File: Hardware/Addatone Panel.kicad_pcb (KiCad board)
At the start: 2 copper layers, 60.8 x 128.5 mm, 36 parts, among them J3 PItch_In, J4 Harm1_In, J5 Harm2_In, J6 Freq_Scale_In, J7 DAC1_Out, J8 DAC2_Out, SW1 SW_Push, SW2 SW_Push, SW3 SW_SPST, SW4 SW_SPST

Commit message: Further updates to PCBs
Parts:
- added G***: LOGO, Graphics:Addatone, B.Cu at (130.0, 45.0)
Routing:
- removed copper zone on B.Cu, net GND
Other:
- board text added: "Fine"
- board text added: "Mountjoy Modular"
- board text added: "Tune"
- board text removed: "+1"
- board text removed: "+2"
- board text removed: "-1"
- board text removed: "-2"
- board text removed: "0"
- board text removed: "Fine Tune"

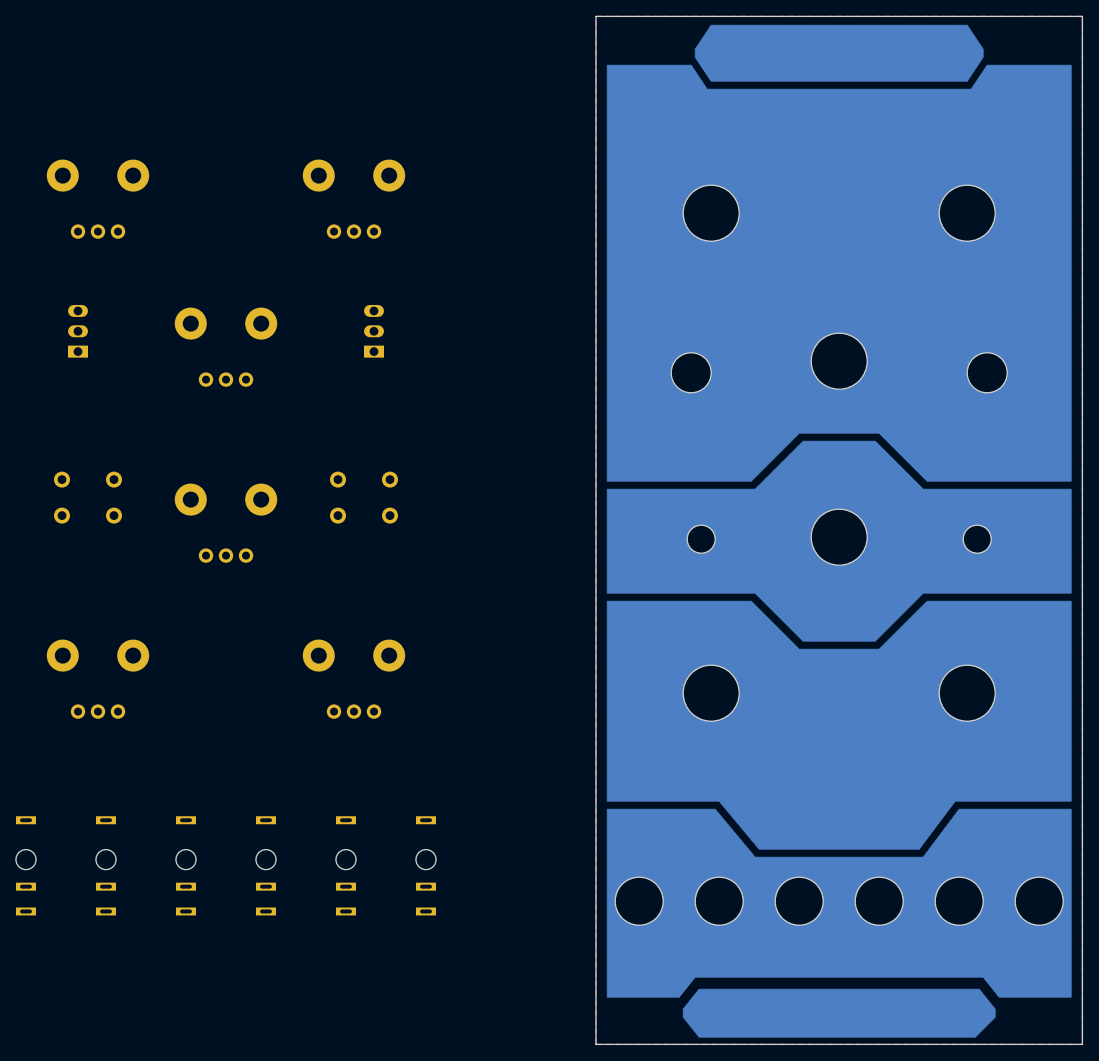
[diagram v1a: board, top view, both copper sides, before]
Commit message: Checking FPGA programming code and updated bitstream
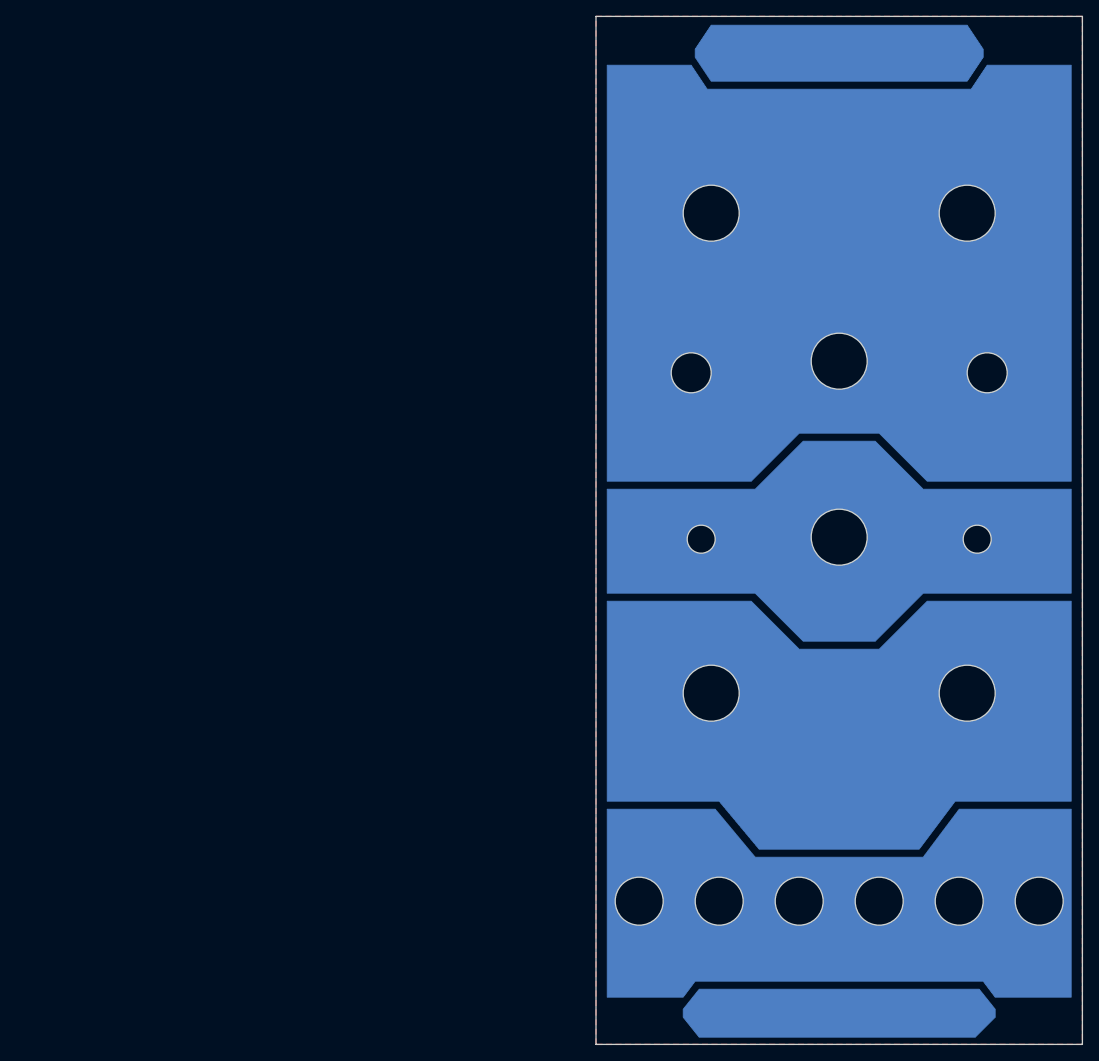
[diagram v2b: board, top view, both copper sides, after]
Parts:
- removed CTune1, FTune1, FreqScale1, Harm1, Harm2, HarmCount1: B10k, Custom_Footprints:Alpha_9mm_Potentiometer
- removed J3: PItch_In, Custom_Footprints:THONKICONN_hole
- removed J4: Harm1_In, Custom_Footprints:THONKICONN_hole
- removed J5: Harm2_In, Custom_Footprints:THONKICONN_hole
- removed J6: Freq_Scale_In, Custom_Footprints:THONKICONN_hole
- removed J7: DAC1_Out, Custom_Footprints:THONKICONN_hole
- removed J8: DAC2_Out, Custom_Footprints:THONKICONN_hole
- removed SW1, SW2: SW_Push, Buttons_Switches_THT:SW_PUSH_6mm
- removed SW3, SW4: SW_SPST, Custom_Footprints:SPDTSubMiniature

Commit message: Updates to PCB layout
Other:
- board text added: "Addatone Panel v1.0"
- board text added: "JLCJLCJLCJLC"
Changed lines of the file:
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@@
   (general
     (thickness 1.6)
-    (drawings 120)
+    (drawings 122)
     (tracks 0)
     (zones 0)
@@
   (page A4)
   (layers
-    (0 F.Cu signal)
-    (31 B.Cu signal)
+    (0 F.Cu signal hide)
+    (31 B.Cu signal hide)
     (32 B.Adhes user)
     (33 F.Adhes user hide)
@@
       (drillshape 0)
       (scaleselection 1)
-      (outputdirectory "Gerbers/PCB/"))
+      (outputdirectory "Gerbers/Panel/"))
   )
   (net 0 "")
@@
     (pad "" np_thru_hole oval (at 0 0) (size 5 3.2) (drill oval 5 3.2) (layers *.Cu *.Mask))
   )
+  (gr_text JLCJLCJLCJLC (at 130.5 161.4) (layer F.SilkS)
+    (effects (font (size 1 1) (thickness 0.15)))
+  )
+  (gr_text "Addatone Panel v1.0" (at 130.2 51.7) (layer F.SilkS)
+    (effects (font (size 2 2) (thickness 0.3)))
+  )
   (gr_line (start 113.4 49.6) (end 146.6 49.6) (layer B.Mask) (width 0.4))

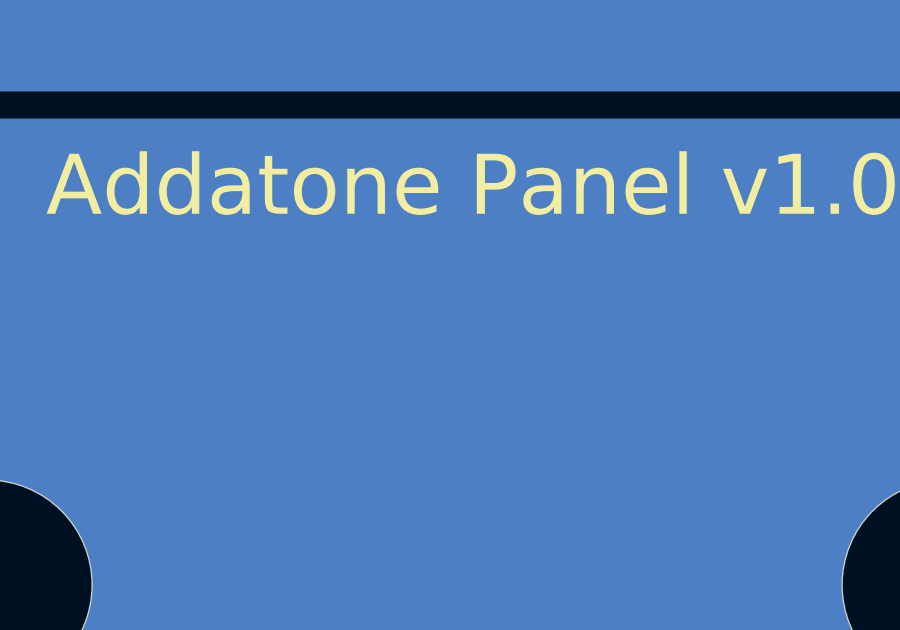
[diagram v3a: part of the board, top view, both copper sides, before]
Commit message: Fixes to schematic (missing resistor on 1.2V LDO); Created new implementation to support production board; added FPGA tester project
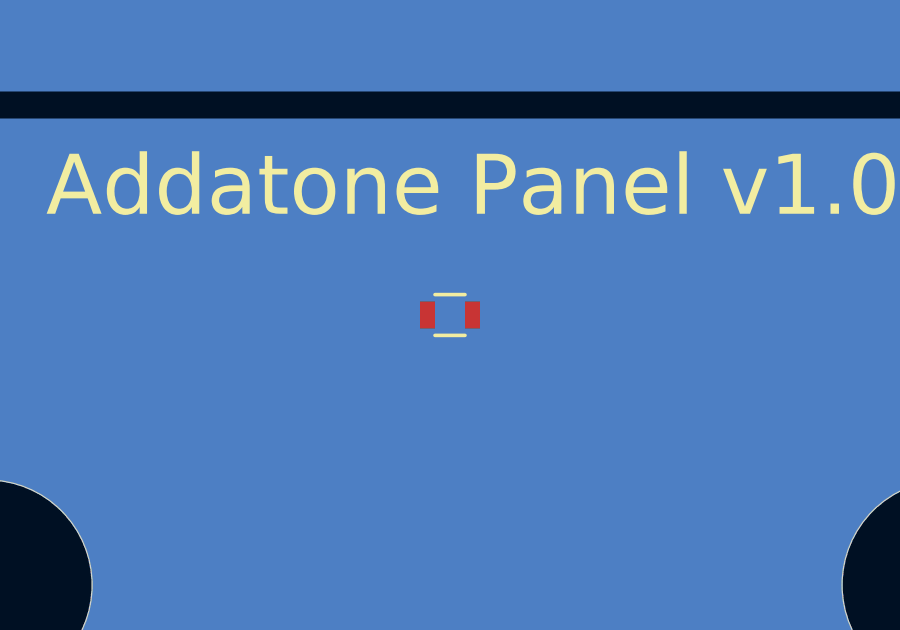
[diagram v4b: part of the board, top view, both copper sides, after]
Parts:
- added REF**: R_0603, Resistors_SMD:R_0603, F.Cu at (129.4, 56.0)
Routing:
- added copper zone on F.Cu, net (none)
- removed copper zone on F.Cu, net GND
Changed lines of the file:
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@@
     (tracks 0)
     (zones 0)
-    (modules 21)
-    (nets 2)
+    (modules 22)
+    (nets 1)
   )
   (page A4)
@@
   )
   (net 0 "")
-  (net 1 GND)
   (net_class Default "This is the default net class."
     (clearance 0.2)
@@
     (uvia_dia 0.3)
     (uvia_drill 0.1)
+  )
+  (module Resistors_SMD:R_0603 (layer F.Cu)
+    (at 129.43 56)
+    (descr "Resistor SMD 0603, reflow soldering, Vishay (see dcrcw.pdf)")
+    (tags "resistor 0603")
+    (attr smd)
+    (fp_text reference REF** (at 0 -1.45) (layer F.SilkS) hide
+      (effects (font (size 1 1) (thickness 0.15)))
+    )
+    (fp_text value R_0603 (at 0 1.5) (layer F.Fab)
+      (effects (font (size 1 1) (thickness 0.15)))
+    )
+    (fp_text user %R (at 0 0) (layer F.Fab)
+      (effects (font (size 0.4 0.4) (thickness 0.075)))
+    )
+    (fp_line (start -0.8 0.4) (end -0.8 -0.4) (layer F.Fab) (width 0.1))
+    (fp_line (start 0.8 0.4) (end -0.8 0.4) (layer F.Fab) (width 0.1))
+    (fp_line (start 0.8 -0.4) (end 0.8 0.4) (layer F.Fab) (width 0.1))
+    (fp_line (start -0.8 -0.4) (end 0.8 -0.4) (layer F.Fab) (width 0.1))
+    (fp_line (start 0.5 0.68) (end -0.5 0.68) (layer F.SilkS) (width 0.12))
+    (fp_line (start -0.5 -0.68) (end 0.5 -0.68) (layer F.SilkS) (width 0.12))
+    (fp_line (start -1.25 -0.7) (end 1.25 -0.7) (layer F.CrtYd) (width 0.05))
+    (fp_line (start -1.25 -0.7) (end -1.25 0.7) (layer F.CrtYd) (width 0.05))
+    (fp_line (start 1.25 0.7) (end 1.25 -0.7) (layer F.CrtYd) (width 0.05))
+    (fp_line (start 1.25 0.7) (end -1.25 0.7) (layer F.CrtYd) (width 0.05))
+    (pad 1 smd rect (at -0.75 0) (size 0.5 0.9) (layers F.Cu F.Paste F.Mask))
+    (pad 2 smd rect (at 0.75 0) (size 0.5 0.9) (layers F.Cu F.Paste F.Mask))
+    (model ${KISYS3DMOD}/Resistors_SMD.3dshapes/R_0603.wrl
+      (at (xyz 0 0 0))
+      (scale (xyz 1 1 1))
+      (rotate (xyz 0 0 0))
+    )
   )
   (module Graphics:Addatone (layer B.Cu)
@@
   (gr_line (start 100 50) (end 100 160) (layer Dwgs.User) (width 0.2))
   (gr_line (start 100 50) (end 160 50) (layer Dwgs.User) (width 0.2))
-  (zone (net 1) (net_name GND) (layer F.Cu) (hatch edge 0.508)
+  (zone (net 0) (net_name "") (layer F.Cu) (hatch edge 0.508)
     (connect_pads (clearance 0.508))
     (min_thickness 0.254)

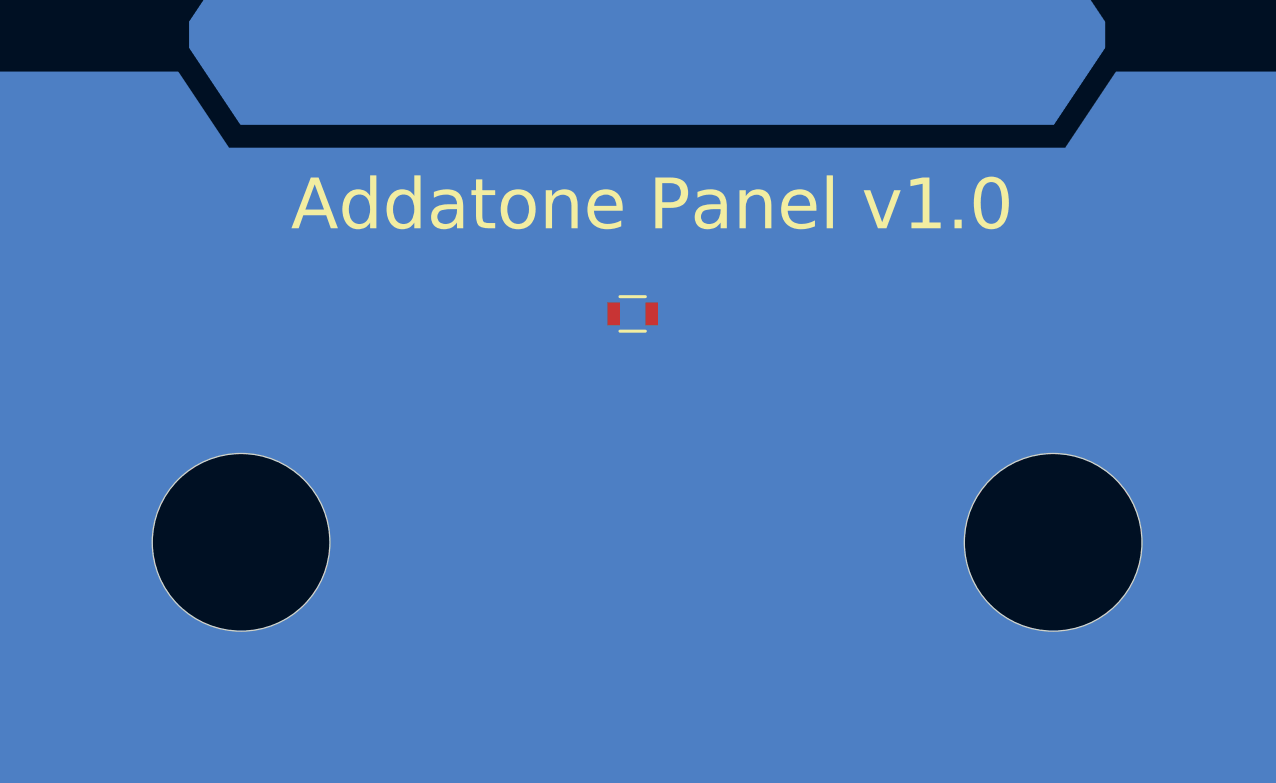
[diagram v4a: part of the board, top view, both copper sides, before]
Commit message: Updated panel; altered controls to use CV to adjust harmonic count
RTL altered to half level of last harmonic to smooth harmonic count CV control
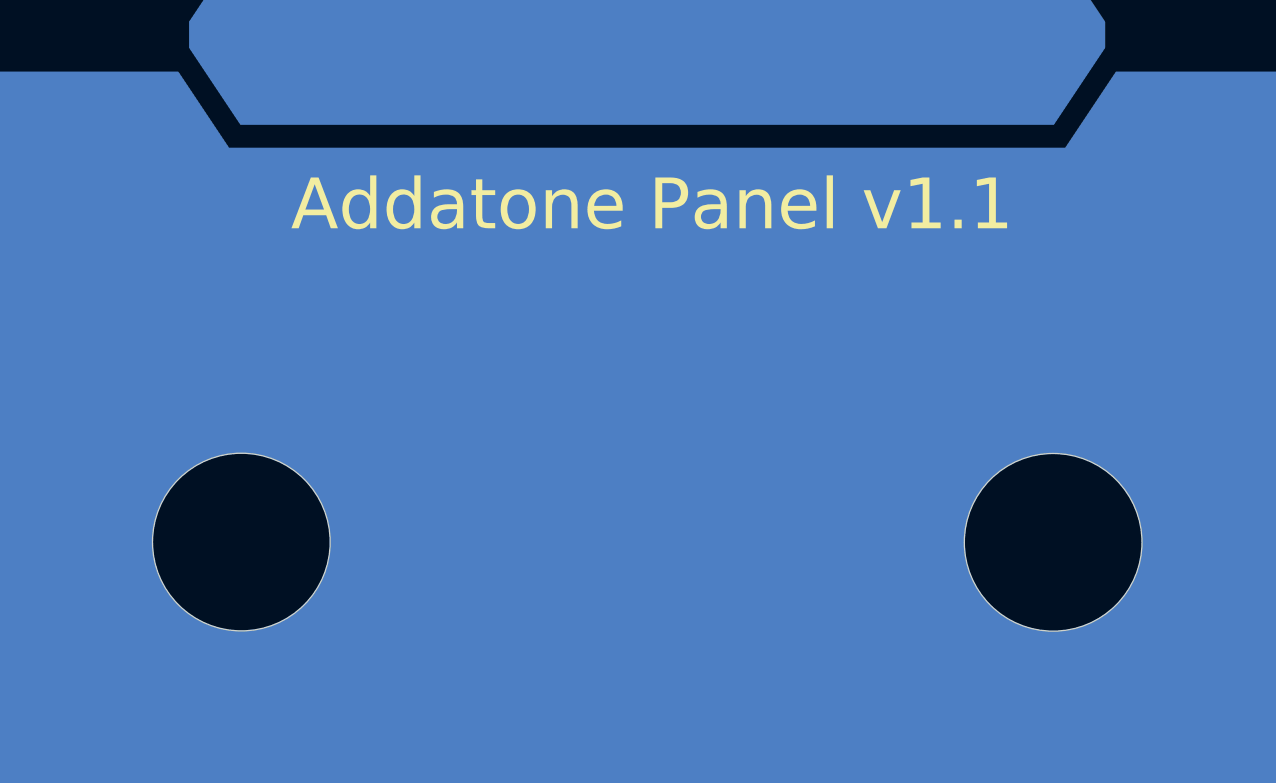
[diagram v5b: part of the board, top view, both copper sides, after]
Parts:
- removed REF**: R_0603, Resistors_SMD:R_0603
- Ref** (x14): moved to B.Cu
- turned Ref** to 180 degrees (x13)
- turned Ref** to -90 degrees
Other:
- net class Default removed
- net class Wide_Power removed
- board text added: "Addatone Panel v1.1"
- board text removed: "Addatone Panel v1.0"
- board text removed: "Warp"

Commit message: Clean up panel pcb
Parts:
- Ref** (x2): moved to B.Cu
- turned Ref** to 180 degrees (x2)
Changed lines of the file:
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@@
   )
   (setup
+    (stackup
+      (layer "F.SilkS" (type "Top Silk Screen") (color "White"))
+      (layer "F.Paste" (type "Top Solder Paste"))
+      (layer "F.Mask" (type "Top Solder Mask") (color "Black") (thickness 0.01))
+      (layer "F.Cu" (type "copper") (thickness 0.035))
+      (layer "dielectric 1" (type "core") (thickness 1.51) (material "FR4") (epsilon_r 4.5) (loss_tangent 0.02))
+      (layer "B.Cu" (type "copper") (thickness 0.035))
+      (layer "B.Mask" (type "Bottom Solder Mask") (color "Black") (thickness 0.01))
+      (layer "B.Paste" (type "Bottom Solder Paste"))
+      (layer "B.SilkS" (type "Bottom Silk Screen") (color "White"))
+      (copper_finish "HAL lead-free")
+      (dielectric_constraints no)
+    )
     (pad_to_mask_clearance 0)
-    (solder_mask_min_width 0.25)
     (pcbplotparams
-      (layerselection 0x00010fc_ffffffff)
+      (layerselection 0x00010f0_ffffffff)
       (disableapertmacros false)
       (usegerberextensions false)
-      (usegerberattributes false)
+      (usegerberattributes true)
       (usegerberadvancedattributes false)
       (creategerberjobfile false)
@@
     (pad "" np_thru_hole oval locked (at 0 0) (size 5 3.2) (drill oval 5 3.2) (layers *.Cu *.Mask))
   )
-  (footprint "Custom_Footprints:Sub_Miniature_Switch_MountingHole_3.5mm" (layer "F.Cu")
-    (at 112.75 105.75)
-    (descr "Mounting Hole 6mm, no annular")
-    (tags "mounting hole 6mm no annular")
-    (attr through_hole)
-    (fp_text reference "Ref**" (at 0 -5.4) (layer "F.SilkS") hide
-      (effects (font (size 1 1) (thickness 0.15)))
-    )
-    (fp_text value "Subminiature_Switch" (at 0 5.1) (layer "F.Fab") hide
-      (effects (font (size 1 1) (thickness 0.15)))
-    )
-    (fp_circle (center 0 0) (end 1.5 0) (layer "Cmts.User") (width 0.15) (fill none))
-    (fp_circle (center 0 0) (end 1.6 0) (layer "F.CrtYd") (width 0.05) (fill none))
-    (pad "" np_thru_hole circle locked (at 0 0) (size 3.5 3.5) (drill 3.5) (layers *.Cu *.Mask))
-  )
-  (footprint "Custom_Footprints:Sub_Miniature_Switch_MountingHole_3.5mm" (layer "F.Cu")
-    (at 147.25 105.75)
-    (descr "Mounting Hole 6mm, no annular")
-    (tags "mounting hole 6mm no annular")
-    (attr through_hole)
-    (fp_text reference "Ref**" (at 0 -5.4) (layer "F.SilkS") hide
-      (effects (font (size 1 1) (thickness 0.15)))
-    )
-    (fp_text value "Subminiature_Switch" (at 0 5.1) (layer "F.Fab") hide
-      (effects (font (size 1 1) (thickness 0.15)))
-    )
-    (fp_circle (center 0 0) (end 1.5 0) (layer "Cmts.User") (width 0.15) (fill none))
-    (fp_circle (center 0 0) (end 1.6 0) (layer "F.CrtYd") (width 0.05) (fill none))
-    (pad "" np_thru_hole circle locked (at 0 0) (size 3.5 3.5) (drill 3.5) (layers *.Cu *.Mask))
-  )
   (footprint "Custom_Footprints:Alpha_9mm_pot_hole" (layer "B.Cu")
     (at 114.01 64.99 180)
@@
       (offset (xyz 0 0 0))
       (scale (xyz 0.87 0.87 0.87))
+      (rotate (xyz 0 0 0))
+    )
+  )
+  (footprint "Custom_Footprints:Sub_Miniature_Switch_MountingHole_3.5mm" (layer "B.Cu")
+    (at 112.75 105.75 180)
+    (descr "Mounting Hole 6mm, no annular")
+    (tags "mounting hole 6mm no annular")
+    (attr through_hole)
+    (fp_text reference "Ref**" (at 0 5.4) (layer "B.SilkS") hide
+      (effects (font (size 1 1) (thickness 0.15)) (justify mirror))
+    )
+    (fp_text value "Subminiature_Switch" (at 0 -5.1) (layer "B.Fab") hide
+      (effects (font (size 1 1) (thickness 0.15)) (justify mirror))
+    )
+    (fp_circle (center 0 0) (end 1.5 0) (layer "Cmts.User") (width 0.15) (fill none))
+    (fp_circle (center 0 0) (end 1.6 0) (layer "B.CrtYd") (width 0.05) (fill none))
+    (pad "" np_thru_hole circle locked (at 0 0 180) (size 3.5 3.5) (drill 3.5) (layers *.Cu *.Mask))
+    (model "${KISYS3DMOD}/Button_Switch_THT.3dshapes/SW_PUSH_6mm_H13mm.wrl"
+      (offset (xyz -3.15 2.25 -11.5))
+      (scale (xyz 1 1 1))
+      (rotate (xyz 0 0 0))
+    )
+  )
+  (footprint "Custom_Footprints:Sub_Miniature_Switch_MountingHole_3.5mm" (layer "B.Cu")
+    (at 147.25 105.75 180)
+    (descr "Mounting Hole 6mm, no annular")
+    (tags "mounting hole 6mm no annular")
+    (attr through_hole)
+    (fp_text reference "Ref**" (at 0 5.4) (layer "B.SilkS") hide
+      (effects (font (size 1 1) (thickness 0.15)) (justify mirror))
+    )
+    (fp_text value "Subminiature_Switch" (at 0 -5.1) (layer "B.Fab") hide
+      (effects (font (size 1 1) (thickness 0.15)) (justify mirror))
+    )
+    (fp_circle (center 0 0) (end 1.5 0) (layer "Cmts.User") (width 0.15) (fill none))
+    (fp_circle (center 0 0) (end 1.6 0) (layer "B.CrtYd") (width 0.05) (fill none))
+    (pad "" np_thru_hole circle locked (at 0 0 180) (size 3.5 3.5) (drill 3.5) (layers *.Cu *.Mask))
+    (model "${KISYS3DMOD}/Button_Switch_THT.3dshapes/SW_PUSH_6mm_H13mm.wrl"
+      (offset (xyz -3.15 2.25 -11.5))
+      (scale (xyz 1 1 1))
       (rotate (xyz 0 0 0))
     )
@@
   (zone (net 0) (net_name "") (layer "F.Cu") (hatch edge 0.508)
     (connect_pads (clearance 0.508))
-    (min_thickness 0.254)
+    (min_thickness 0.254) (filled_areas_thickness no)
     (fill yes (thermal_gap 0.508) (thermal_bridge_width 0.508))
     (polygon
